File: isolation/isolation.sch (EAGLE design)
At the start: 81 parts, among them IC1 XTLV61048DBVR, IC2 SN74HC14PWR, IC3 SN74HCS32BQAR, IC4 SN74HCS08DYYR, IC5 FDN359BN, IC6 FDN359BN, IC7 FDN359BN, IC8 FDN359BN, J1 S4B-PH-K-S(LF)(SN), J2 S4B-PH-K-S(LF)(SN), J3 S4B-PH-K-S(LF)(SN), J4 S4B-PH-K-S(LF)(SN), J5 S4B-PH-K-S(LF)(SN)

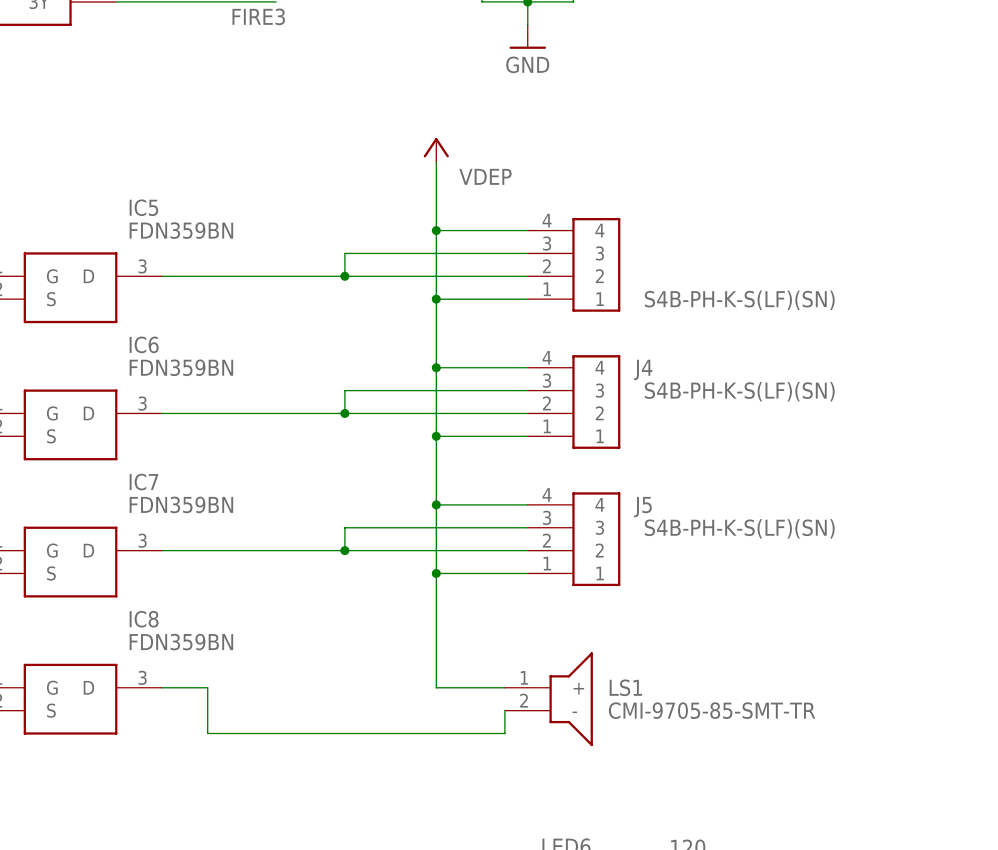
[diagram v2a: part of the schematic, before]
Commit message: 2 pin ignitor connectors
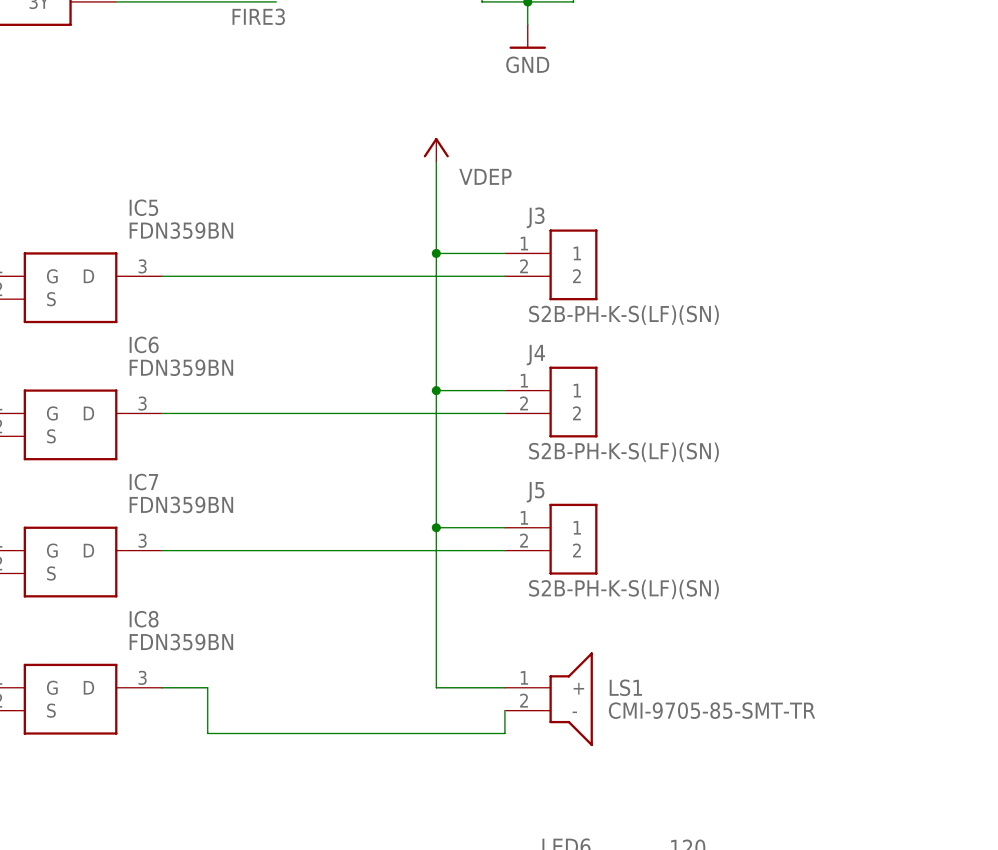
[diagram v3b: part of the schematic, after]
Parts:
- J3, J4, J5: value S4B-PH-K-S(LF)(SN) -> S2B-PH-K-S(LF)(SN); device Headers:S4B-PH-K-S(LF)(SN) -> Connectors:S2B-PH-K-S(LF)(SN)
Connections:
- removed net N$19: IC6.D, J4.2, J4.3
- removed net N$20: IC7.D, J5.2, J5.3
- new net N$14: IC7.D, J5.2
- new net N$15: IC6.D, J4.2
- net N$17: no longer J3.3
- net VDEP: no longer J3.4, J4.4, J5.4
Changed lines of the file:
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@@
 <part name="SUPPLY22" library="Power_Symbols" library_urn="urn:adsk.eagle:library:16502351" deviceset="GND-BAR" device="" value="GND"/>
 <part name="SUPPLY23" library="Power_Symbols" library_urn="urn:adsk.eagle:library:16502351" deviceset="GND-BAR" device="" value="GND"/>
-<part name="J3" library="Headers" library_urn="urn:adsk.eagle:library:11687645" deviceset="S4B-PH-K-S(LF)(SN)" device="" package3d_urn="urn:adsk.eagle:package:19181369/5"/>
-<part name="J4" library="Headers" library_urn="urn:adsk.eagle:library:11687645" deviceset="S4B-PH-K-S(LF)(SN)" device="" package3d_urn="urn:adsk.eagle:package:19181369/5"/>
-<part name="J5" library="Headers" library_urn="urn:adsk.eagle:library:11687645" deviceset="S4B-PH-K-S(LF)(SN)" device="" package3d_urn="urn:adsk.eagle:package:19181369/5"/>
 <part name="P+1" library="supply1" library_urn="urn:adsk.eagle:library:371" deviceset="VCC" device=""/>
 <part name="R8" library="Resistor" library_urn="urn:adsk.eagle:library:16378527" deviceset="R" device="CHIP-0603(1608-METRIC)" package3d_urn="urn:adsk.eagle:package:16378565/5" technology="_" value="68k"/>
@@
 <part name="TP1" library="testpad" library_urn="urn:adsk.eagle:library:385" deviceset="TP" device="PAD1-20Y" package3d_urn="urn:adsk.eagle:package:27951/1"/>
 <part name="TP2" library="testpad" library_urn="urn:adsk.eagle:library:385" deviceset="TP" device="PAD1-20Y" package3d_urn="urn:adsk.eagle:package:27951/1"/>
+<part name="J3" library="Connectors" library_urn="urn:adsk.eagle:library:14555660" deviceset="S2B-PH-K-S(LF)(SN)" device="" package3d_urn="urn:adsk.eagle:package:10989924/2"/>
+<part name="J4" library="Connectors" library_urn="urn:adsk.eagle:library:14555660" deviceset="S2B-PH-K-S(LF)(SN)" device="" package3d_urn="urn:adsk.eagle:package:10989924/2"/>
+<part name="J5" library="Connectors" library_urn="urn:adsk.eagle:library:14555660" deviceset="S2B-PH-K-S(LF)(SN)" device="" package3d_urn="urn:adsk.eagle:package:10989924/2"/>
 </parts>
 <sheets>
@@
 <attribute name="VALUE" x="-1.905" y="-340.36" size="1.778" layer="96" rot="R270" align="center"/>
 </instance>
-<instance part="J3" gate="G$1" x="104.14" y="-289.56" smashed="yes" rot="R180">
-<attribute name="VALUE" x="130.81" y="-294.64" size="1.778" layer="96" rot="R180" align="center-left"/>
-</instance>
-<instance part="J4" gate="G$1" x="104.14" y="-304.8" smashed="yes" rot="R180">
-<attribute name="NAME" x="110.49" y="-302.26" size="1.778" layer="95" rot="R180" align="center-left"/>
-<attribute name="VALUE" x="130.81" y="-304.8" size="1.778" layer="96" rot="R180" align="center-left"/>
-</instance>
-<instance part="J5" gate="G$1" x="104.14" y="-320.04" smashed="yes" rot="R180">
-<attribute name="NAME" x="110.49" y="-317.5" size="1.778" layer="95" rot="R180" align="center-left"/>
-<attribute name="VALUE" x="130.81" y="-320.04" size="1.778" layer="96" rot="R180" align="center-left"/>
-</instance>
 <instance part="P+1" gate="VCC" x="86.36" y="-276.86" smashed="yes"/>
 <instance part="R8" gate="G$1" x="20.32" y="-284.48" smashed="yes" rot="R180">
@@
 <attribute name="NAME" x="-3.81" y="21.59" size="1.778" layer="95" rot="R90"/>
 <attribute name="TP_SIGNAL_NAME" x="-1.27" y="24.13" size="1.778" layer="97" rot="R90"/>
+</instance>
+<instance part="J3" gate="G$1" x="101.6" y="-289.56" smashed="yes">
+<attribute name="NAME" x="96.52" y="-286.258" size="1.778" layer="95"/>
+<attribute name="VALUE" x="96.52" y="-297.18" size="1.778" layer="96"/>
+</instance>
+<instance part="J4" gate="G$1" x="101.6" y="-304.8" smashed="yes">
+<attribute name="NAME" x="96.52" y="-301.498" size="1.778" layer="95"/>
+<attribute name="VALUE" x="96.52" y="-312.42" size="1.778" layer="96"/>
+</instance>
+<instance part="J5" gate="G$1" x="101.6" y="-320.04" smashed="yes">
+<attribute name="NAME" x="96.52" y="-316.738" size="1.778" layer="95"/>
+<attribute name="VALUE" x="96.52" y="-327.66" size="1.778" layer="96"/>
 </instance>
 </instances>
@@
 <wire x1="93.98" y1="-337.82" x2="86.36" y2="-337.82" width="0.1524" layer="91"/>
 <pinref part="P+1" gate="VCC" pin="VCC"/>
-<wire x1="86.36" y1="-337.82" x2="86.36" y2="-325.12" width="0.1524" layer="91"/>
-<pinref part="J3" gate="G$1" pin="4"/>
-<wire x1="86.36" y1="-325.12" x2="86.36" y2="-317.5" width="0.1524" layer="91"/>
-<wire x1="86.36" y1="-317.5" x2="86.36" y2="-309.88" width="0.1524" layer="91"/>
-<wire x1="86.36" y1="-309.88" x2="86.36" y2="-302.26" width="0.1524" layer="91"/>
-<wire x1="86.36" y1="-302.26" x2="86.36" y2="-294.64" width="0.1524" layer="91"/>
-<wire x1="86.36" y1="-294.64" x2="86.36" y2="-287.02" width="0.1524" layer="91"/>
-<wire x1="86.36" y1="-287.02" x2="86.36" y2="-279.4" width="0.1524" layer="91"/>
-<wire x1="96.52" y1="-287.02" x2="86.36" y2="-287.02" width="0.1524" layer="91"/>
-<junction x="86.36" y="-287.02"/>
+<wire x1="86.36" y1="-337.82" x2="86.36" y2="-320.04" width="0.1524" layer="91"/>
+<label x="88.9" y="-281.94" size="1.778" layer="95"/>
 <pinref part="J3" gate="G$1" pin="1"/>
-<wire x1="96.52" y1="-294.64" x2="86.36" y2="-294.64" width="0.1524" layer="91"/>
-<junction x="86.36" y="-294.64"/>
-<pinref part="J4" gate="G$1" pin="4"/>
-<wire x1="96.52" y1="-302.26" x2="86.36" y2="-302.26" width="0.1524" layer="91"/>
-<junction x="86.36" y="-302.26"/>
-<pinref part="J5" gate="G$1" pin="4"/>
-<wire x1="96.52" y1="-317.5" x2="86.36" y2="-317.5" width="0.1524" layer="91"/>
-<junction x="86.36" y="-317.5"/>
+<wire x1="86.36" y1="-320.04" x2="86.36" y2="-304.8" width="0.1524" layer="91"/>
+<wire x1="86.36" y1="-304.8" x2="86.36" y2="-289.56" width="0.1524" layer="91"/>
+<wire x1="86.36" y1="-289.56" x2="86.36" y2="-279.4" width="0.1524" layer="91"/>
+<wire x1="93.98" y1="-289.56" x2="86.36" y2="-289.56" width="0.1524" layer="91"/>
+<junction x="86.36" y="-289.56"/>
+<pinref part="J4" gate="G$1" pin="1"/>
+<wire x1="93.98" y1="-304.8" x2="86.36" y2="-304.8" width="0.1524" layer="91"/>
+<junction x="86.36" y="-304.8"/>
 <pinref part="J5" gate="G$1" pin="1"/>
-<wire x1="96.52" y1="-325.12" x2="86.36" y2="-325.12" width="0.1524" layer="91"/>
-<junction x="86.36" y="-325.12"/>
-<label x="88.9" y="-281.94" size="1.778" layer="95"/>
-<pinref part="J4" gate="G$1" pin="1"/>
-<wire x1="96.52" y1="-309.88" x2="86.36" y2="-309.88" width="0.1524" layer="91"/>
-<junction x="86.36" y="-309.88"/>
+<wire x1="93.98" y1="-320.04" x2="86.36" y2="-320.04" width="0.1524" layer="91"/>
+<junction x="86.36" y="-320.04"/>
 </segment>
 </net>
@@
 <segment>
 <pinref part="IC5" gate="G$1" pin="D"/>
+<wire x1="55.88" y1="-292.1" x2="93.98" y2="-292.1" width="0.1524" layer="91"/>
 <pinref part="J3" gate="G$1" pin="2"/>
-<wire x1="55.88" y1="-292.1" x2="76.2" y2="-292.1" width="0.1524" layer="91"/>
-<pinref part="J3" gate="G$1" pin="3"/>
-<wire x1="76.2" y1="-292.1" x2="96.52" y2="-292.1" width="0.1524" layer="91"/>
-<wire x1="96.52" y1="-289.56" x2="76.2" y2="-289.56" width="0.1524" layer="91"/>
-<wire x1="76.2" y1="-289.56" x2="76.2" y2="-292.1" width="0.1524" layer="91"/>
-<junction x="76.2" y="-292.1"/>
-</segment>
-</net>
-<net name="N$19" class="0">
-<segment>
-<pinref part="IC6" gate="G$1" pin="D"/>
-<pinref part="J4" gate="G$1" pin="2"/>
-<wire x1="55.88" y1="-307.34" x2="76.2" y2="-307.34" width="0.1524" layer="91"/>
-<pinref part="J4" gate="G$1" pin="3"/>
-<wire x1="76.2" y1="-307.34" x2="96.52" y2="-307.34" width="0.1524" layer="91"/>
-<wire x1="96.52" y1="-304.8" x2="76.2" y2="-304.8" width="0.1524" layer="91"/>
-<wire x1="76.2" y1="-304.8" x2="76.2" y2="-307.34" width="0.1524" layer="91"/>
-<junction x="76.2" y="-307.34"/>
-</segment>
-</net>
-<net name="N$20" class="0">
-<segment>
-<pinref part="IC7" gate="G$1" pin="D"/>
-<pinref part="J5" gate="G$1" pin="2"/>
-<wire x1="55.88" y1="-322.58" x2="76.2" y2="-322.58" width="0.1524" layer="91"/>
-<pinref part="J5" gate="G$1" pin="3"/>
-<wire x1="76.2" y1="-322.58" x2="96.52" y2="-322.58" width="0.1524" layer="91"/>
-<wire x1="96.52" y1="-320.04" x2="76.2" y2="-320.04" width="0.1524" layer="91"/>
-<wire x1="76.2" y1="-320.04" x2="76.2" y2="-322.58" width="0.1524" layer="91"/>
-<junction x="76.2" y="-322.58"/>
 </segment>
 </net>
@@
 </segment>
 </net>
+<net name="N$14" class="0">
+<segment>
+<pinref part="J5" gate="G$1" pin="2"/>
+<pinref part="IC7" gate="G$1" pin="D"/>
+<wire x1="93.98" y1="-322.58" x2="55.88" y2="-322.58" width="0.1524" layer="91"/>
+</segment>
+</net>
+<net name="N$15" class="0">
+<segment>
+<pinref part="J4" gate="G$1" pin="2"/>
+<pinref part="IC6" gate="G$1" pin="D"/>
+<wire x1="93.98" y1="-307.34" x2="55.88" y2="-307.34" width="0.1524" layer="91"/>
+</segment>
+</net>

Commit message: add test pads
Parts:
- removed JP1, JP2, JP3: (no value), pinhead:PINHD-1X2
- added TP3, TP4, TP5, TP6, TP7, TP8, TP9: PTR1PAD1-13, testpad:PTR1PAD1-13
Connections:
- net FIRE1: now also TP4.TP; no longer JP1.1
- net FIRE2: now also TP6.TP; no longer JP2.1
- net FIRE3: now also TP8.TP; no longer JP3.1
- net VBAT: now also TP3.TP, TP5.TP, TP7.TP; no longer JP1.2, JP2.2, JP3.2
- net VDEP: now also TP9.TP
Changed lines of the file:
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@@
 <part name="R23" library="Resistor" library_urn="urn:adsk.eagle:library:16378527" deviceset="R" device="CHIP-0603(1608-METRIC)" package3d_urn="urn:adsk.eagle:package:16378565/5" technology="_" value="120"/>
 <part name="SUPPLY27" library="Power_Symbols" library_urn="urn:adsk.eagle:library:16502351" deviceset="GND-BAR" device="" value="GND"/>
-<part name="JP1" library="pinhead" library_urn="urn:adsk.eagle:library:325" deviceset="PINHD-1X2" device="" package3d_urn="urn:adsk.eagle:package:22435/2"/>
-<part name="JP2" library="pinhead" library_urn="urn:adsk.eagle:library:325" deviceset="PINHD-1X2" device="" package3d_urn="urn:adsk.eagle:package:22435/2"/>
-<part name="JP3" library="pinhead" library_urn="urn:adsk.eagle:library:325" deviceset="PINHD-1X2" device="" package3d_urn="urn:adsk.eagle:package:22435/2"/>
 <part name="TP1" library="testpad" library_urn="urn:adsk.eagle:library:385" deviceset="TP" device="PAD1-20Y" package3d_urn="urn:adsk.eagle:package:27951/1"/>
 <part name="TP2" library="testpad" library_urn="urn:adsk.eagle:library:385" deviceset="TP" device="PAD1-20Y" package3d_urn="urn:adsk.eagle:package:27951/1"/>
@@
 <part name="J4" library="Connectors" library_urn="urn:adsk.eagle:library:14555660" deviceset="S2B-PH-K-S(LF)(SN)" device="" package3d_urn="urn:adsk.eagle:package:10989924/2"/>
 <part name="J5" library="Connectors" library_urn="urn:adsk.eagle:library:14555660" deviceset="S2B-PH-K-S(LF)(SN)" device="" package3d_urn="urn:adsk.eagle:package:10989924/2"/>
+<part name="TP3" library="testpad" library_urn="urn:adsk.eagle:library:385" deviceset="PTR1" device="PAD1-13" package3d_urn="urn:adsk.eagle:package:27946/1"/>
+<part name="TP4" library="testpad" library_urn="urn:adsk.eagle:library:385" deviceset="PTR1" device="PAD1-13" package3d_urn="urn:adsk.eagle:package:27946/1"/>
+<part name="TP5" library="testpad" library_urn="urn:adsk.eagle:library:385" deviceset="PTR1" device="PAD1-13" package3d_urn="urn:adsk.eagle:package:27946/1"/>
+<part name="TP6" library="testpad" library_urn="urn:adsk.eagle:library:385" deviceset="PTR1" device="PAD1-13" package3d_urn="urn:adsk.eagle:package:27946/1"/>
+<part name="TP7" library="testpad" library_urn="urn:adsk.eagle:library:385" deviceset="PTR1" device="PAD1-13" package3d_urn="urn:adsk.eagle:package:27946/1"/>
+<part name="TP8" library="testpad" library_urn="urn:adsk.eagle:library:385" deviceset="PTR1" device="PAD1-13" package3d_urn="urn:adsk.eagle:package:27946/1"/>
+<part name="TP9" library="testpad" library_urn="urn:adsk.eagle:library:385" deviceset="PTR1" device="PAD1-13" package3d_urn="urn:adsk.eagle:package:27946/1"/>
 </parts>
 <sheets>
@@
 <attribute name="VALUE" x="133.985" y="-419.1" size="1.778" layer="96" rot="R90" align="center"/>
 </instance>
-<instance part="JP1" gate="G$1" x="45.72" y="-403.86" smashed="yes" rot="R180">
-<attribute name="NAME" x="52.07" y="-409.575" size="1.778" layer="95" rot="R180"/>
-<attribute name="VALUE" x="52.07" y="-398.78" size="1.778" layer="96" rot="R180"/>
-</instance>
-<instance part="JP2" gate="G$1" x="45.72" y="-416.56" smashed="yes" rot="R180">
-<attribute name="NAME" x="52.07" y="-422.275" size="1.778" layer="95" rot="R180"/>
-<attribute name="VALUE" x="52.07" y="-411.48" size="1.778" layer="96" rot="R180"/>
-</instance>
-<instance part="JP3" gate="G$1" x="45.72" y="-429.26" smashed="yes" rot="R180">
-<attribute name="NAME" x="52.07" y="-434.975" size="1.778" layer="95" rot="R180"/>
-<attribute name="VALUE" x="52.07" y="-424.18" size="1.778" layer="96" rot="R180"/>
-</instance>
 <instance part="TP1" gate="G$1" x="-5.08" y="50.8" smashed="yes" rot="R90">
 <attribute name="NAME" x="-6.35" y="49.53" size="1.778" layer="95" rot="R90"/>
@@
 <attribute name="NAME" x="96.52" y="-316.738" size="1.778" layer="95"/>
 <attribute name="VALUE" x="96.52" y="-327.66" size="1.778" layer="96"/>
+</instance>
+<instance part="TP3" gate="G$1" x="40.64" y="-401.32" smashed="yes" rot="R270">
+<attribute name="NAME" x="34.29" y="-400.304" size="1.778" layer="95"/>
+<attribute name="TP_SIGNAL_NAME" x="38.1" y="-402.59" size="1.778" layer="97" rot="R270"/>
+</instance>
+<instance part="TP4" gate="G$1" x="40.64" y="-406.4" smashed="yes" rot="R270">
+<attribute name="NAME" x="34.29" y="-405.384" size="1.778" layer="95"/>
+<attribute name="TP_SIGNAL_NAME" x="38.1" y="-407.67" size="1.778" layer="97" rot="R270"/>
+</instance>
+<instance part="TP5" gate="G$1" x="40.64" y="-414.02" smashed="yes" rot="R270">
+<attribute name="NAME" x="34.29" y="-413.004" size="1.778" layer="95"/>
+<attribute name="TP_SIGNAL_NAME" x="38.1" y="-415.29" size="1.778" layer="97" rot="R270"/>
+</instance>
+<instance part="TP6" gate="G$1" x="40.64" y="-419.1" smashed="yes" rot="R270">
+<attribute name="NAME" x="29.21" y="-418.084" size="1.778" layer="95"/>
+<attribute name="TP_SIGNAL_NAME" x="38.1" y="-420.37" size="1.778" layer="97" rot="R270"/>
+</instance>
+<instance part="TP7" gate="G$1" x="40.64" y="-426.72" smashed="yes" rot="R270">
+<attribute name="NAME" x="34.29" y="-425.704" size="1.778" layer="95"/>
+<attribute name="TP_SIGNAL_NAME" x="38.1" y="-427.99" size="1.778" layer="97" rot="R270"/>
+</instance>
+<instance part="TP8" gate="G$1" x="40.64" y="-431.8" smashed="yes" rot="R270">
+<attribute name="NAME" x="34.29" y="-430.784" size="1.778" layer="95"/>
+<attribute name="TP_SIGNAL_NAME" x="38.1" y="-433.07" size="1.778" layer="97" rot="R270"/>
+</instance>
+<instance part="TP9" gate="G$1" x="53.34" y="33.02" smashed="yes" rot="R270">
+<attribute name="NAME" x="46.99" y="34.036" size="1.778" layer="95"/>
+<attribute name="TP_SIGNAL_NAME" x="50.8" y="31.75" size="1.778" layer="97" rot="R270"/>
 </instance>
 </instances>
@@
 </segment>
 <segment>
-<pinref part="JP1" gate="G$1" pin="2"/>
-<wire x1="48.26" y1="-403.86" x2="60.96" y2="-403.86" width="0.1524" layer="91"/>
-<wire x1="60.96" y1="-403.86" x2="60.96" y2="-416.56" width="0.1524" layer="91"/>
-<pinref part="JP3" gate="G$1" pin="2"/>
-<wire x1="60.96" y1="-416.56" x2="60.96" y2="-429.26" width="0.1524" layer="91"/>
-<wire x1="60.96" y1="-429.26" x2="60.96" y2="-441.96" width="0.1524" layer="91"/>
-<wire x1="48.26" y1="-429.26" x2="60.96" y2="-429.26" width="0.1524" layer="91"/>
-<junction x="60.96" y="-429.26"/>
-<pinref part="JP2" gate="G$1" pin="2"/>
-<wire x1="48.26" y1="-416.56" x2="60.96" y2="-416.56" width="0.1524" layer="91"/>
-<junction x="60.96" y="-416.56"/>
+<wire x1="60.96" y1="-401.32" x2="60.96" y2="-414.02" width="0.1524" layer="91"/>
 <label x="63.5" y="-441.96" size="1.778" layer="95"/>
+<pinref part="TP3" gate="G$1" pin="TP"/>
+<wire x1="60.96" y1="-414.02" x2="60.96" y2="-426.72" width="0.1524" layer="91"/>
+<wire x1="60.96" y1="-426.72" x2="60.96" y2="-441.96" width="0.1524" layer="91"/>
+<wire x1="60.96" y1="-401.32" x2="43.18" y2="-401.32" width="0.1524" layer="91"/>
+<pinref part="TP5" gate="G$1" pin="TP"/>
+<wire x1="43.18" y1="-414.02" x2="60.96" y2="-414.02" width="0.1524" layer="91"/>
+<junction x="60.96" y="-414.02"/>
+<pinref part="TP7" gate="G$1" pin="TP"/>
+<wire x1="43.18" y1="-426.72" x2="60.96" y2="-426.72" width="0.1524" layer="91"/>
+<junction x="60.96" y="-426.72"/>
 </segment>
 </net>
@@
 <label x="60.96" y="35.56" size="1.778" layer="95"/>
 <pinref part="C2" gate="G$1" pin="2"/>
-<wire x1="71.12" y1="33.02" x2="63.5" y2="33.02" width="0.1524" layer="91"/>
 <wire x1="71.12" y1="43.18" x2="71.12" y2="33.02" width="0.1524" layer="91"/>
 <junction x="71.12" y="33.02"/>
 <pinref part="R2" gate="G$1" pin="1"/>
 <wire x1="71.12" y1="33.02" x2="71.12" y2="25.4" width="0.1524" layer="91"/>
+<pinref part="TP9" gate="G$1" pin="TP"/>
+<wire x1="71.12" y1="33.02" x2="55.88" y2="33.02" width="0.1524" layer="91"/>
 </segment>
 <segment>
@@
 <segment>
 <pinref part="LED12" gate="G$1" pin="A"/>
-<wire x1="96.52" y1="-411.48" x2="73.66" y2="-411.48" width="0.1524" layer="91"/>
 <label x="78.74" y="-411.48" size="1.778" layer="95"/>
-<pinref part="JP1" gate="G$1" pin="1"/>
-<wire x1="48.26" y1="-406.4" x2="73.66" y2="-406.4" width="0.1524" layer="91"/>
-<wire x1="73.66" y1="-406.4" x2="73.66" y2="-411.48" width="0.1524" layer="91"/>
+<wire x1="96.52" y1="-411.48" x2="50.8" y2="-411.48" width="0.1524" layer="91"/>
+<wire x1="50.8" y1="-411.48" x2="50.8" y2="-406.4" width="0.1524" layer="91"/>
+<pinref part="TP4" gate="G$1" pin="TP"/>
+<wire x1="50.8" y1="-406.4" x2="43.18" y2="-406.4" width="0.1524" layer="91"/>
 </segment>
 </net>
@@
 <pinref part="LED13" gate="G$1" pin="A"/>
 <label x="78.74" y="-419.1" size="1.778" layer="95"/>
-<pinref part="JP2" gate="G$1" pin="1"/>
-<wire x1="48.26" y1="-419.1" x2="96.52" y2="-419.1" width="0.1524" layer="91"/>
+<wire x1="43.18" y1="-419.1" x2="96.52" y2="-419.1" width="0.1524" layer="91"/>
+<pinref part="TP6" gate="G$1" pin="TP"/>
 </segment>
 </net>
@@
 <segment>
 <pinref part="LED14" gate="G$1" pin="A"/>
-<wire x1="96.52" y1="-426.72" x2="73.66" y2="-426.72" width="0.1524" layer="91"/>
 <label x="78.74" y="-426.72" size="1.778" layer="95"/>
-<pinref part="JP3" gate="G$1" pin="1"/>
-<wire x1="48.26" y1="-431.8" x2="73.66" y2="-431.8" width="0.1524" layer="91"/>
-<wire x1="73.66" y1="-431.8" x2="73.66" y2="-426.72" width="0.1524" layer="91"/>
-</segment>
-</net>
+<wire x1="96.52" y1="-426.72" x2="66.04" y2="-426.72" width="0.1524" layer="91"/>
+<wire x1="66.04" y1="-426.72" x2="66.04" y2="-431.8" width="0.1524" layer="91"/>
+<pinref part="TP8" gate="G$1" pin="TP"/>
+<wire x1="66.04" y1="-431.8" x2="43.18" y2="-431.8" width="0.1524" layer="91"/>
+</segment>
+</net>
